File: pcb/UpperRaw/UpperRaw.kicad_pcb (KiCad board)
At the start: 2 copper layers, 52 x 63 mm, 12 parts, among them J1 Conn_01x04, SW100 SW_DPDT_x2, SW101 SW_DPDT_x2

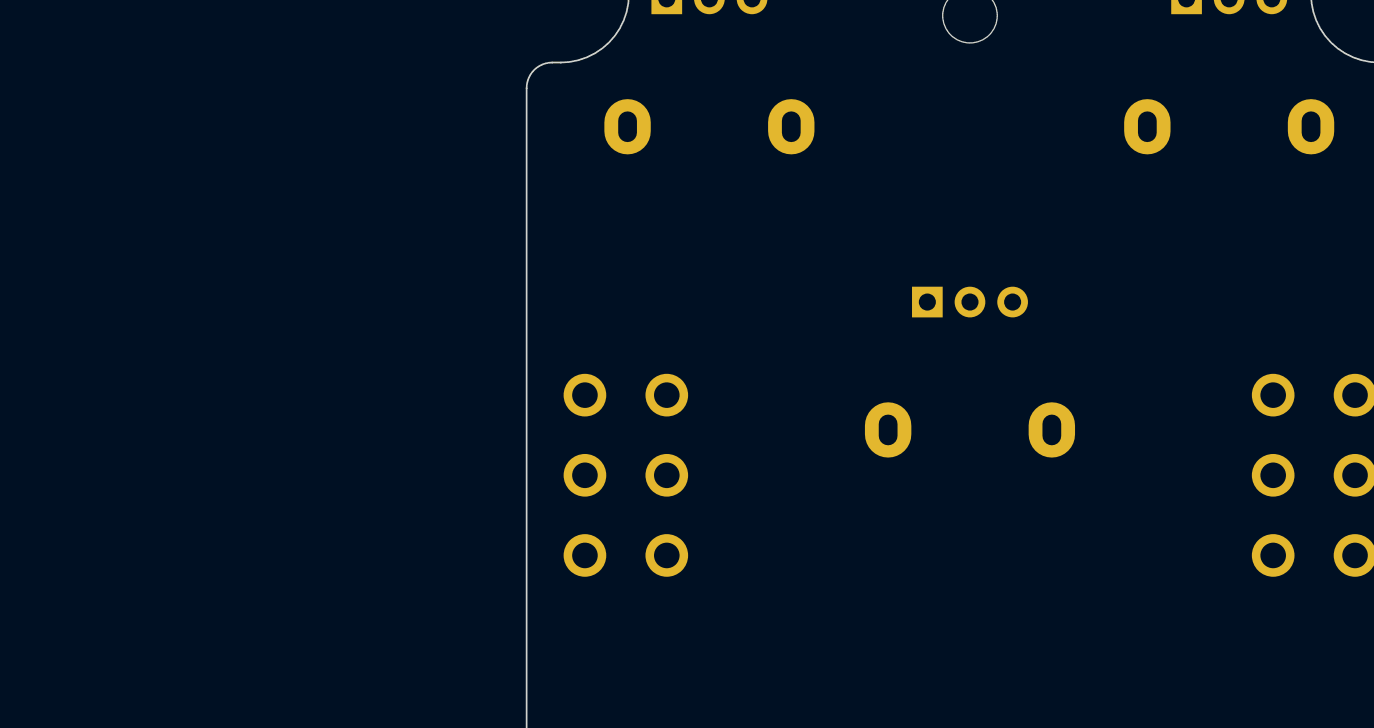
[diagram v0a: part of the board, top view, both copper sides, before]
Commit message: [UpperRaw] Add symbols from 404 PCB
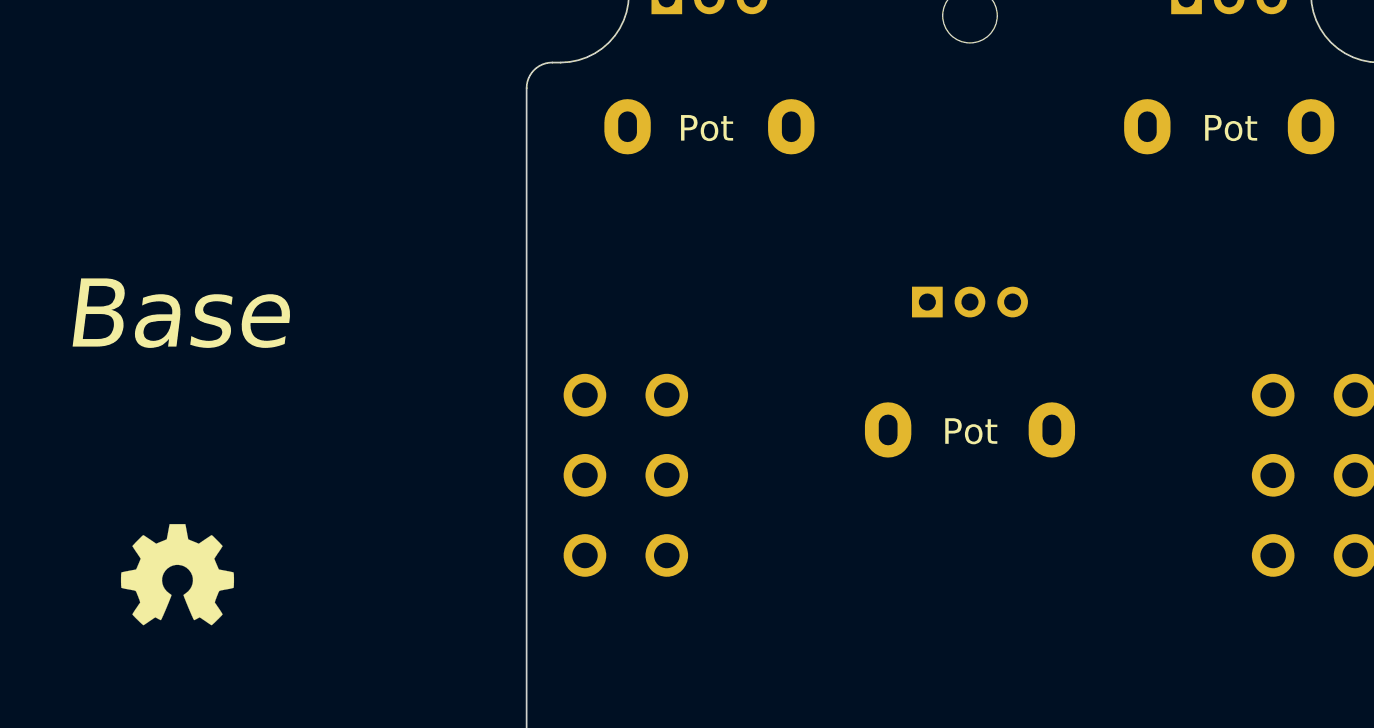
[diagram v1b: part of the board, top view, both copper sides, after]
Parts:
- added REF**: OSHW-Symbol_6.7x6mm_SilkScreen, Symbol:OSHW-Symbol_6.7x6mm_SilkScreen, F.Cu at (103.0, 103.5)
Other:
- board text added: "Base"
- board text added: "Pot"

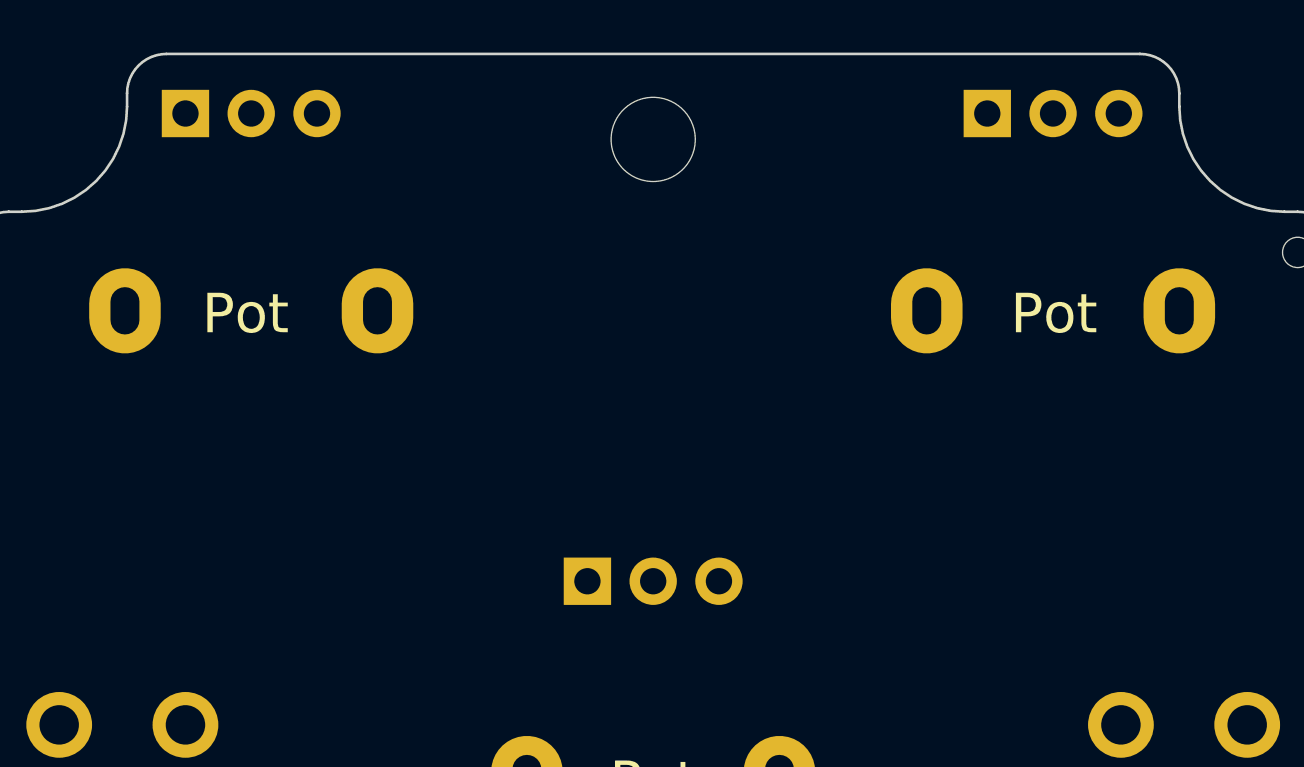
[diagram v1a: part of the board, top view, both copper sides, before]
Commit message: [All] Update all pot footprints and silkscreens
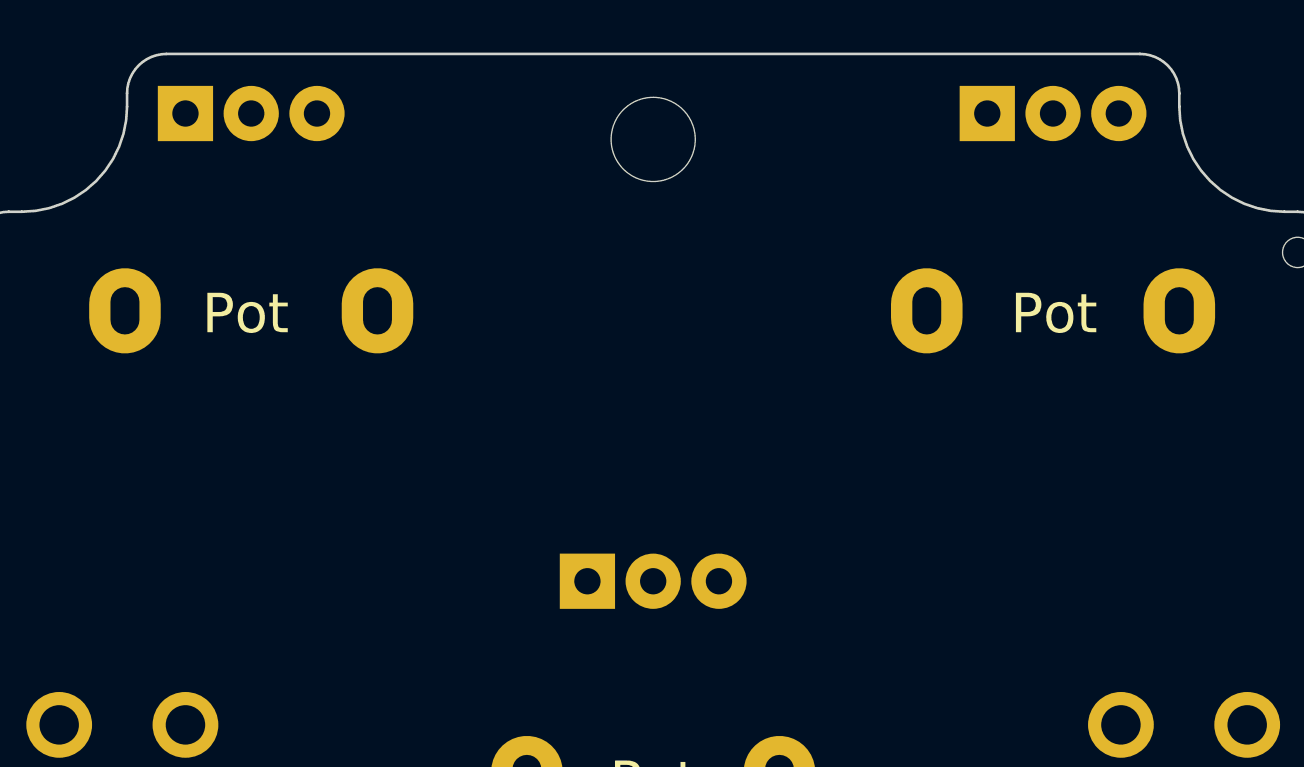
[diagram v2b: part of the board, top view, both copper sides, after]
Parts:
- RV100, RV101, RV102: footprint Potentiometer_THT:Potentiometer_Alpha_RD901F-40-00D_Single_Vertical -> MeineBib:Potentiometer_Alpha_RD901F-40-00D_Single_Vertical

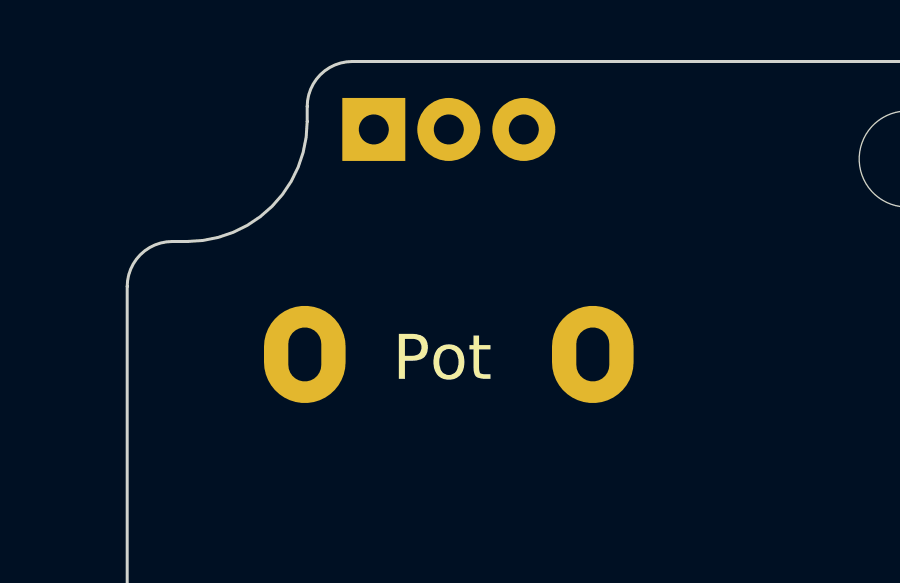
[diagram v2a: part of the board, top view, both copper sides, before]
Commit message: [All] Find out that the upper left pot is 0,08mm off on all designs
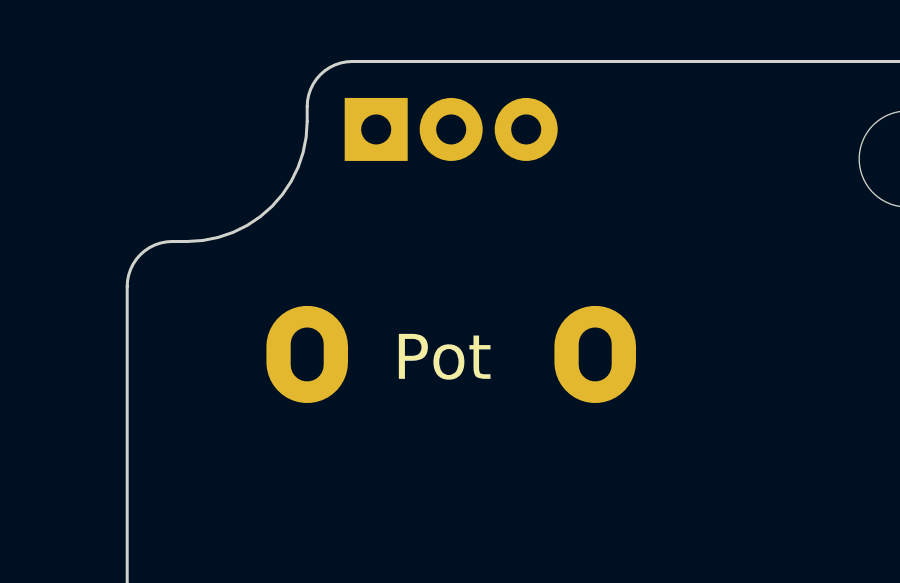
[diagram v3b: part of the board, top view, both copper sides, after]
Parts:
- moved RV101 0.08 mm to (131.8, 69.8)
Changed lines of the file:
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@@
   )
   (footprint "MeineBib:Potentiometer_Alpha_RD901F-40-00D_Single_Vertical" (layer "B.Cu")
-    (at 131.72 69.765 -90)
+    (at 131.8 69.765 -90)
     (descr "Potentiometer, vertical, 9mm, single, http://www.taiwanalpha.com.tw/downloads?target=products&id=113")
     (tags "potentiometer vertical 9mm single")

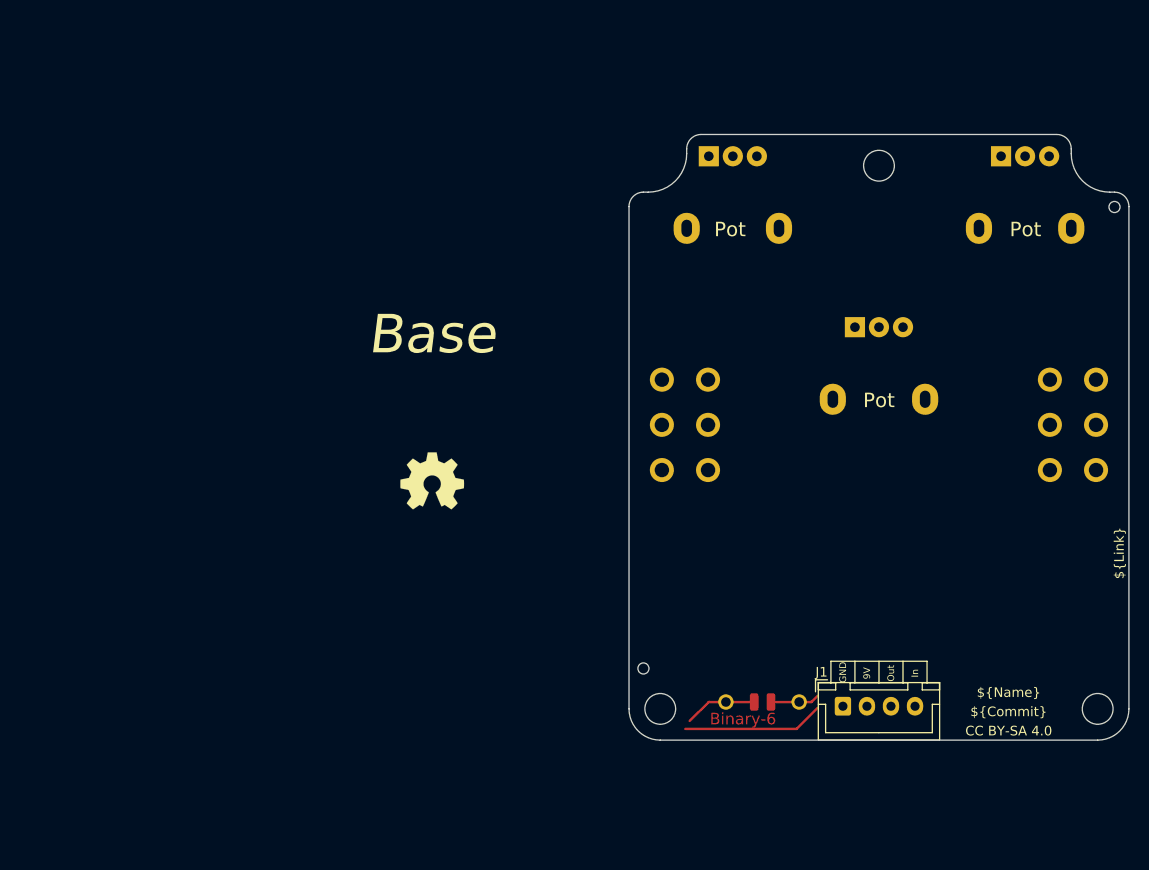
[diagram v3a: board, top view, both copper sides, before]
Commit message: [UpperRaw] Figure out new pot positions for 6 pots
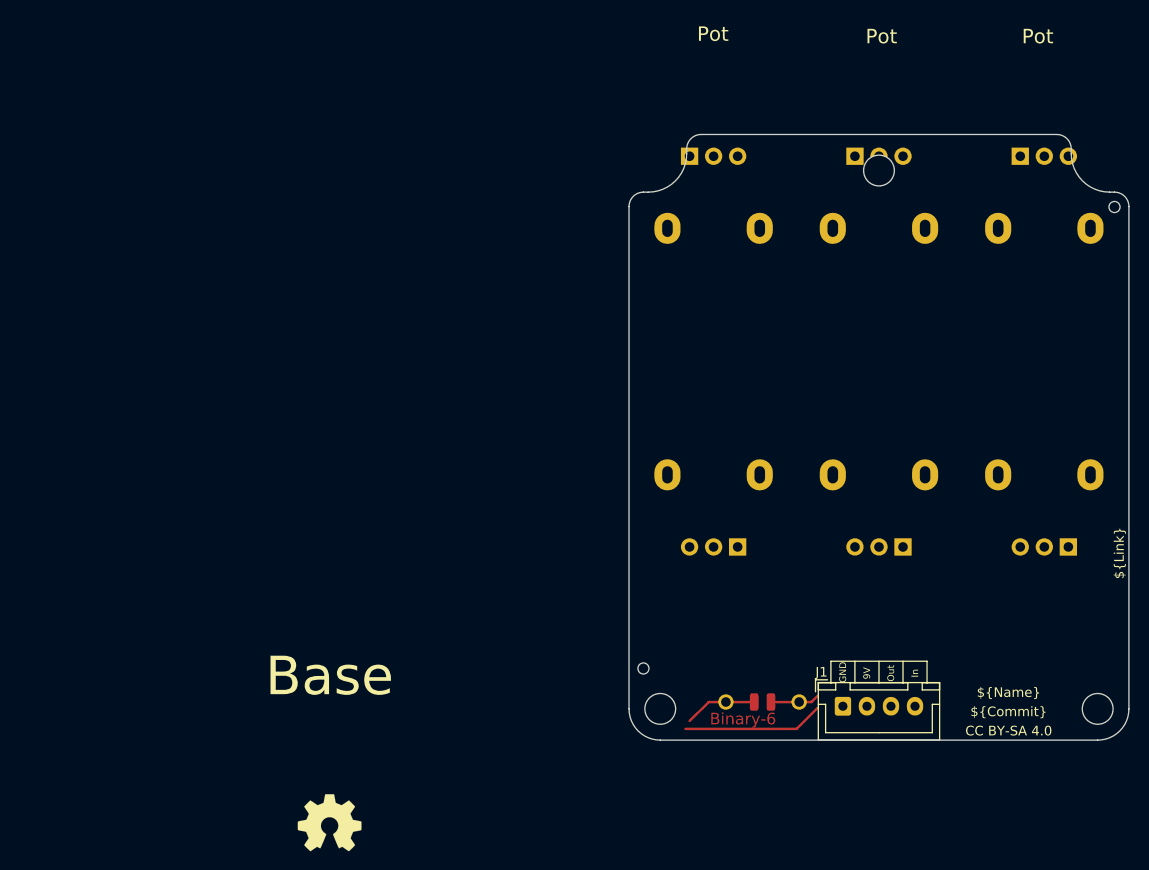
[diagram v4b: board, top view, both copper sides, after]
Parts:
- removed SW100, SW101: SW_DPDT_x2, MeineBib:Switch_toggle_DPDT_Print
- added RV200: 100K Lin, Potentiometer_THT:Potentiometer_Alpha_RD901F-40-00D_Single_Vertical, B.Cu at (134.8, 110.4)
- added RV201: 100K Lin, Potentiometer_THT:Potentiometer_Alpha_RD901F-40-00D_Single_Vertical, B.Cu at (152.0, 110.4)
- added RV202: 100K Lin, Potentiometer_THT:Potentiometer_Alpha_RD901F-40-00D_Single_Vertical, B.Cu at (169.2, 110.4)
- RV100, RV101, RV102: footprint MeineBib:Potentiometer_Alpha_RD901F-40-00D_Single_Vertical -> Potentiometer_THT:Potentiometer_Alpha_RD901F-40-00D_Single_Vertical
- moved REF** 37.1 mm to (92.3, 139.1)
- moved RV100 24.7 mm to (129.8, 69.8)
- moved RV101 15.2 mm to (147.0, 69.8)
- moved RV102 2.00 mm to (164.2, 69.8)
- moved MK2 0.50 mm to (149.5, 71.2)

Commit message: [AllRaw] Update base templates to 6 controls design
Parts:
- added REF**: OSHW-Symbol_6.7x6mm_SilkScreen, Symbol:OSHW-Symbol_6.7x6mm_SilkScreen, B.Cu at (149.5, 116.8)
- moved REF** 61.3 mm to (149.5, 116.8)
- moved MK2 6.02 mm to (149.5, 77.3)
- moved REF** 1.55 mm to (174.0, 73.5)
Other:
- outline, holes or cut-outs redrawn
- board text added: "Either delete mounting hole or pot"

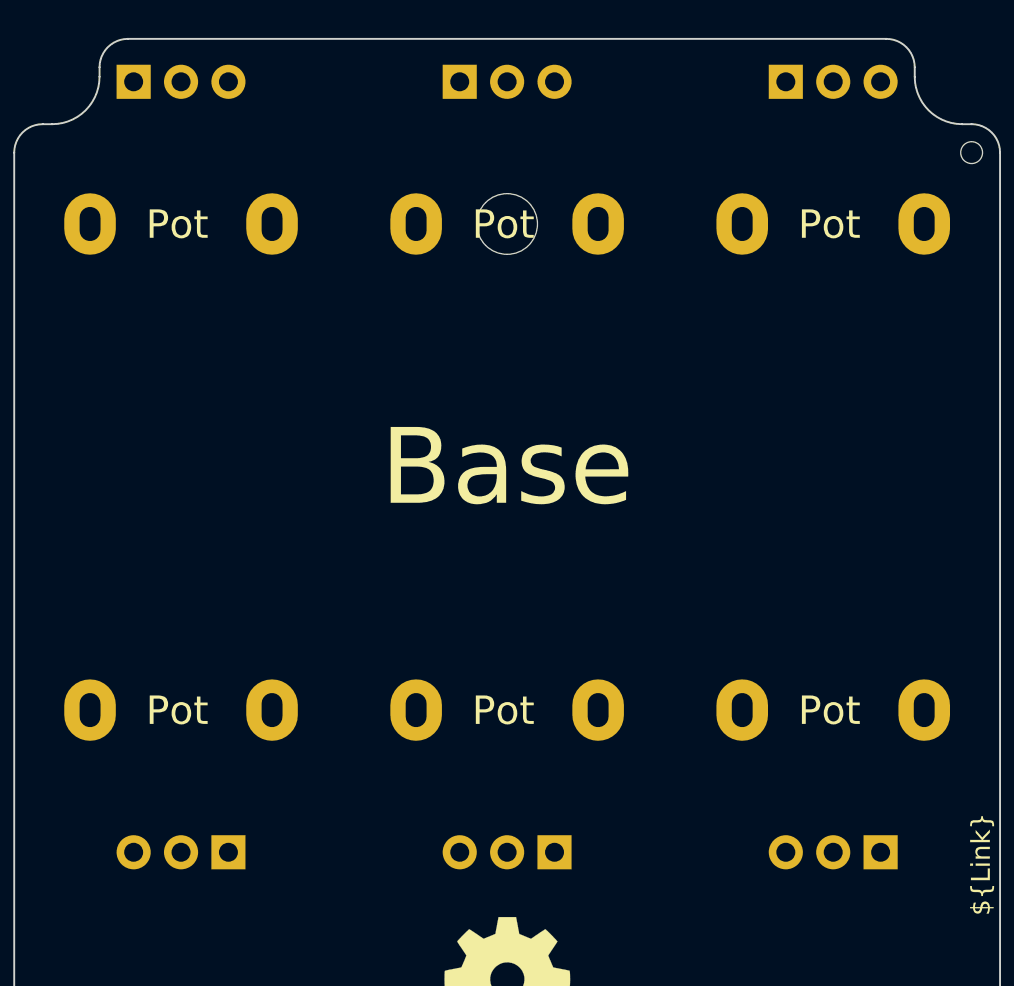
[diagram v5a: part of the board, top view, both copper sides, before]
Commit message: [UpperRaw] Swap pot footprints
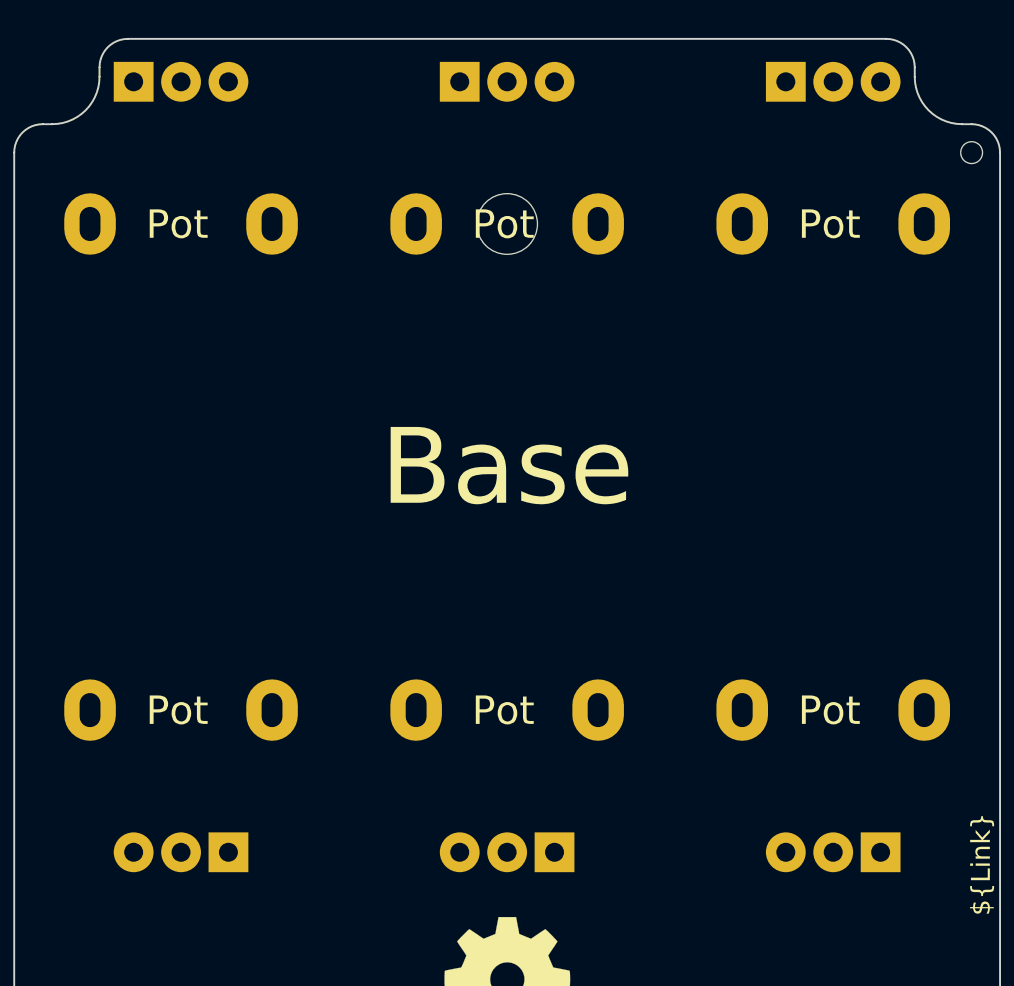
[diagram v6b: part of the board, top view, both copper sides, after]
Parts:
- RV100, RV101, RV102, RV200, RV201, RV202: footprint Potentiometer_THT:Potentiometer_Alpha_RD901F-40-00D_Single_Vertical -> MeineBib:Potentiometer_Alpha_RD901F-40-00D_Single_Vertical
